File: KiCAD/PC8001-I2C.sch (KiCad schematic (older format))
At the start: 43 parts, among them J1 ADDR-JP, J2 I2C RTC DS3231, J3 I2C OUT, J4 PC8001 Ext Con, J5 I2C ExtOUT1, J6 I2C ExtOUT1, J7 I2C ExtOUT1, J8 I2C ExtOUT1, Q1 2N7000, U1 74HC138, U2 DS1307+, U3 8255, U4 24LC1025, U5 24LC1025, U6 74HC07, U7 74HC4051, U8 74LS32, Y1 32.768kHz

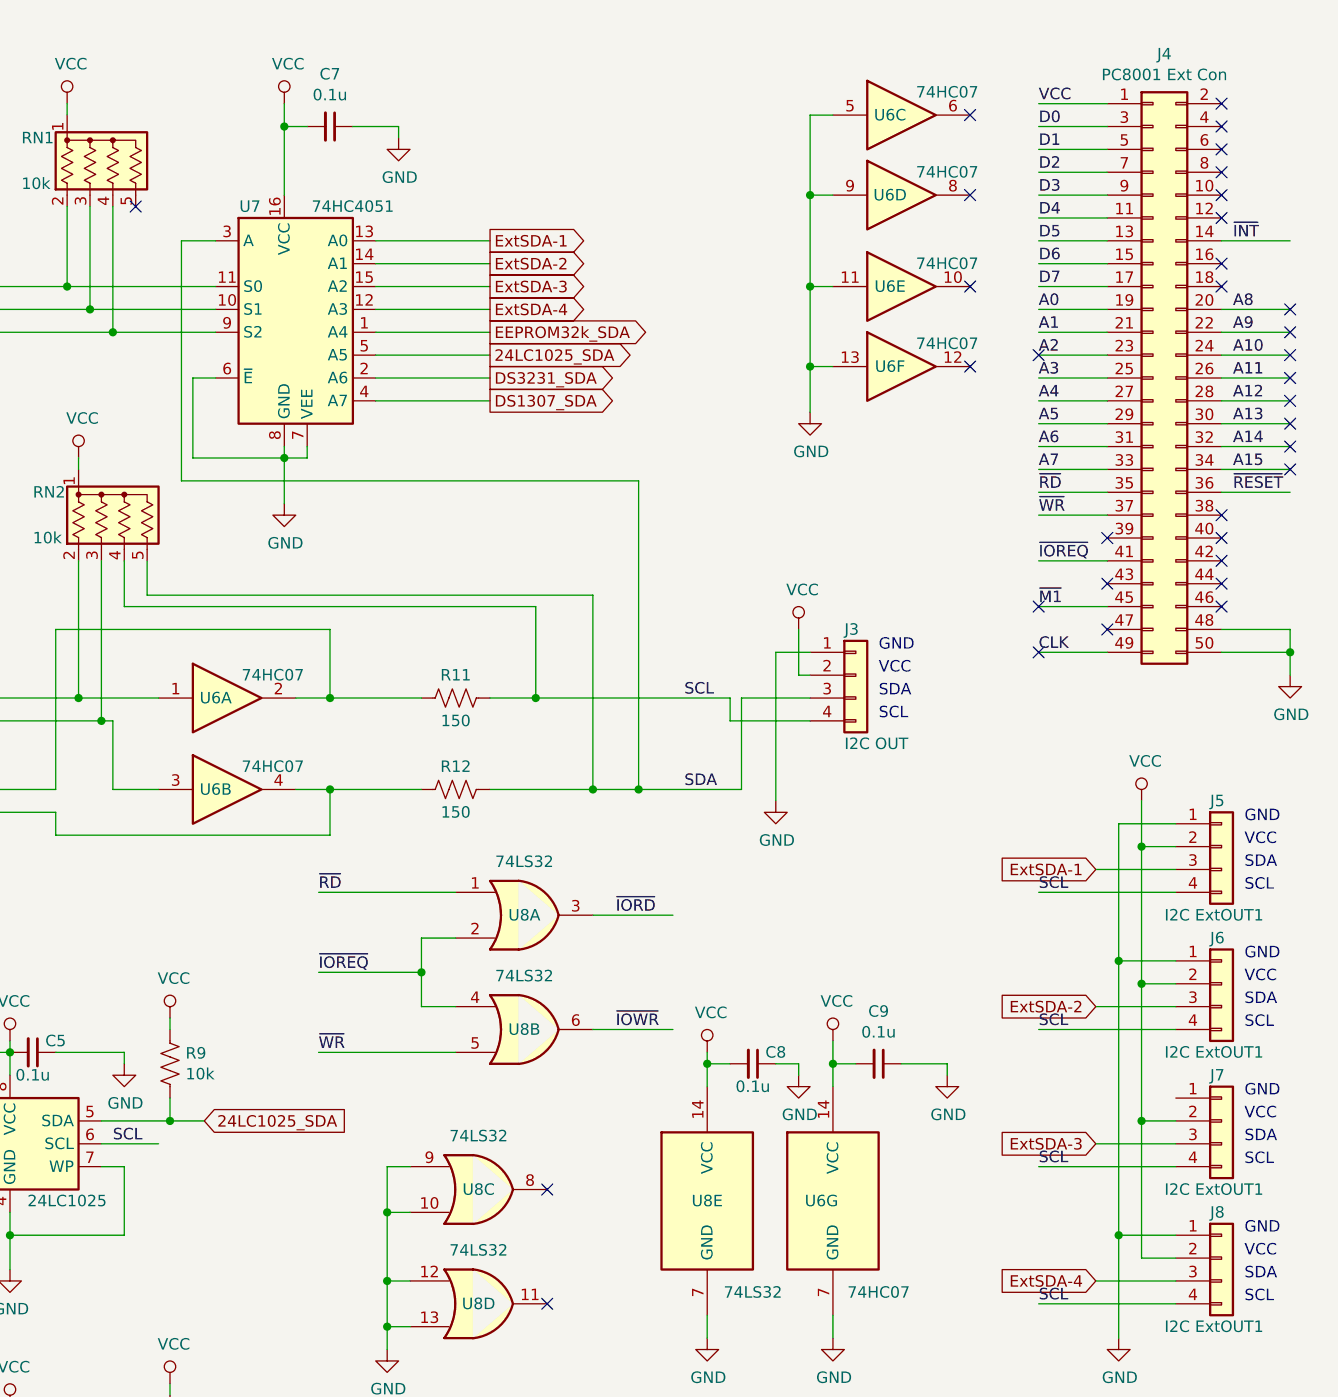
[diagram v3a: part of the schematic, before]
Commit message: 外部I2C端子へ74HC07追加
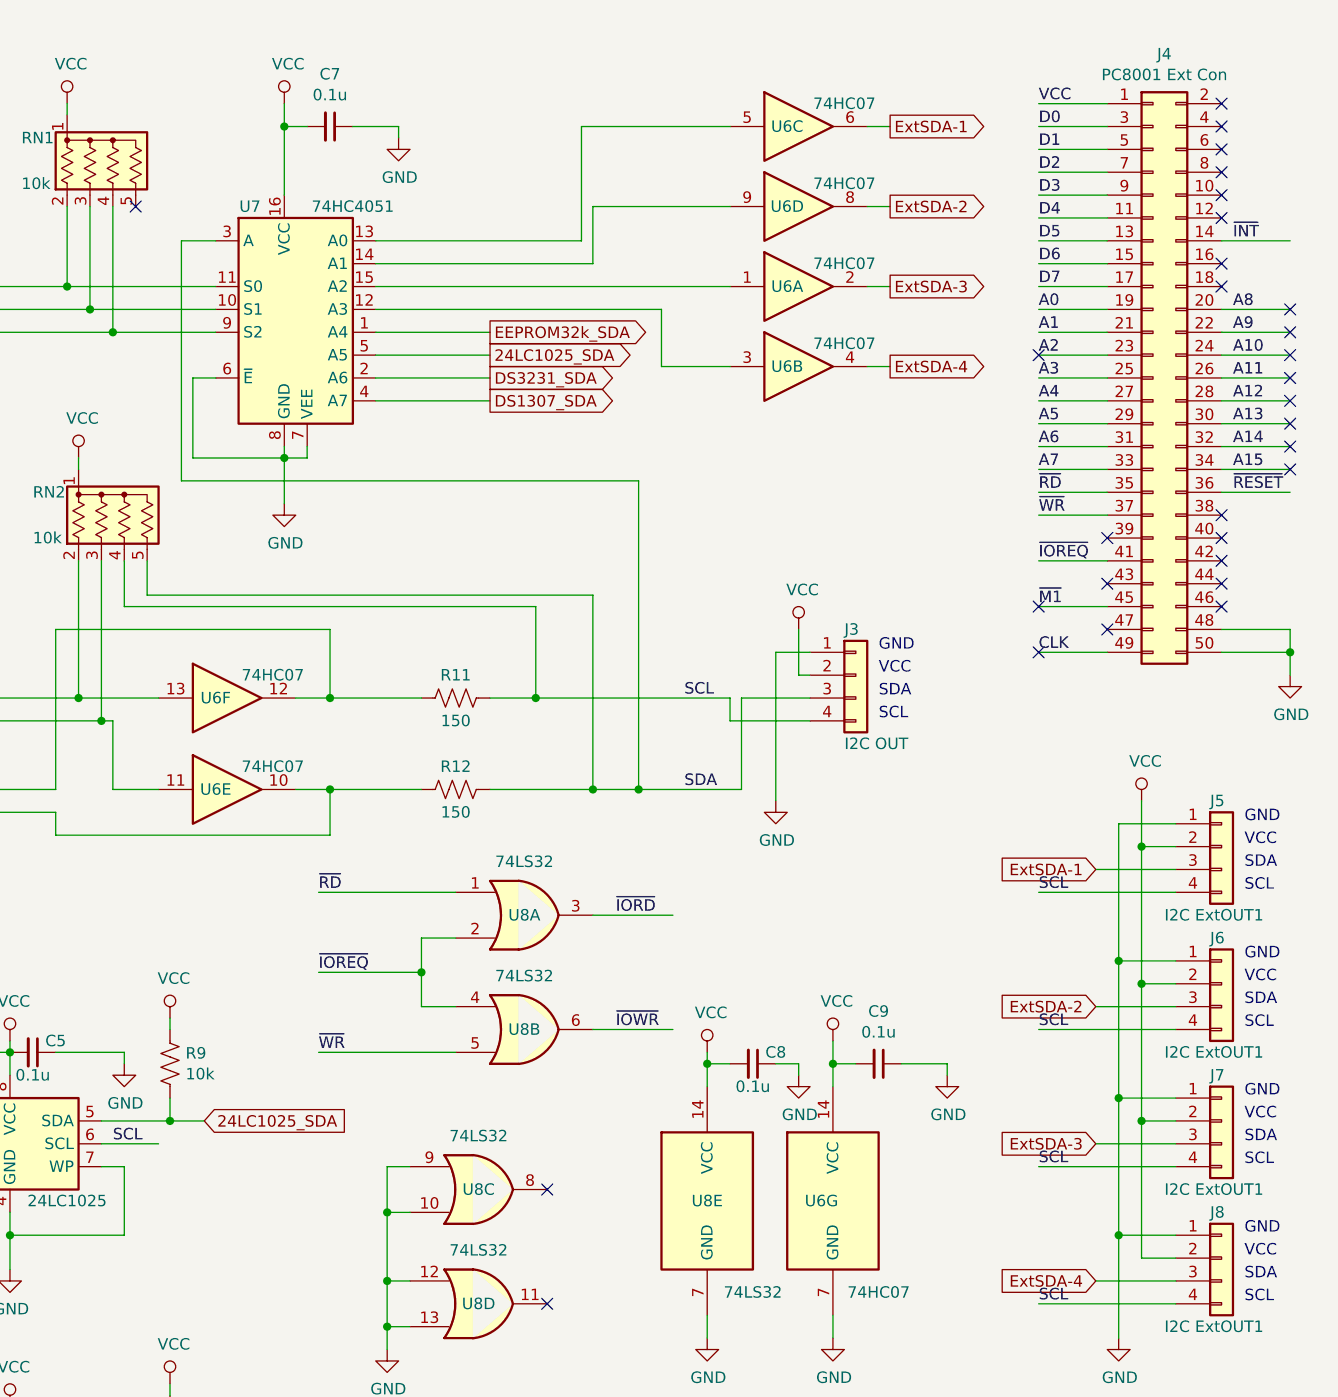
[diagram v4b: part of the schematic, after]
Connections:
- net ExtSDA-1: now also U6.6; no longer U7.13 (A0)
- net ExtSDA-2: now also U6.8; no longer U7.14 (A1)
- net ExtSDA-3: now also U6.2; no longer U7.15 (A2)
- net ExtSDA-4: now also U6.4; no longer U7.12 (A3)
- net GND: now also J7.1 (Pin_1); no longer U6.11, U6.13, U6.5, U6.9
- net at R11.1, U3.13 (PC4): now also U6.12; no longer U6.2
- net at R12.1, U3.12 (PC5): now also U6.10; no longer U6.4
- net at RN2.2 (R1), U3.14 (PC0): now also U6.13; no longer U6.1
- net at RN2.3 (R2), U3.15 (PC1): now also U6.11; no longer U6.3
- new net: U6.1, U7.15 (A2)
- new net: U6.3, U7.12 (A3)
- new net: U6.5, U7.13 (A0)
- new net: U6.9, U7.14 (A1)
- no-connect marks 51 -> 47
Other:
- moved on the sheet: U6A, U6B, U6C, U6D, U6E, U6F
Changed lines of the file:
@@
 Text GLabel 7600 2100 2    50   Output ~ 0
 DS1307_SDA
-Wire Wire Line
-	7100 1700 7600 1700
-Wire Wire Line
-	7100 1600 7600 1600
-Wire Wire Line
-	7100 1500 7600 1500
-Wire Wire Line
-	7100 1400 7600 1400
 Text GLabel 7600 1900 2    50   Output ~ 0
 24LC1025_SDA
@@
 L 74xx:74LS07 U6
 U 1 1 5E8C9365
-P 6450 3400
-F 0 "U6" H 6400 3400 50  0000 C CNN
-F 1 "74HC07" H 6650 3500 50  0000 C CNN
-F 2 "" H 6450 3400 50  0001 C CNN
-F 3 "www.ti.com/lit/ds/symlink/sn74ls07.pdf" H 6450 3400 50  0001 C CNN
-	1    6450 3400
+P 8950 1600
+F 0 "U6" H 8900 1600 50  0000 C CNN
+F 1 "74HC07" H 9150 1700 50  0000 C CNN
+F 2 "" H 8950 1600 50  0001 C CNN
+F 3 "www.ti.com/lit/ds/symlink/sn74ls07.pdf" H 8950 1600 50  0001 C CNN
+	1    8950 1600
 	1    0    0    -1
 $EndComp
@@
 L 74xx:74LS07 U6
 U 2 1 5E8CAB8D
-P 6450 3800
-F 0 "U6" H 6400 3800 50  0000 C CNN
-F 1 "74HC07" H 6650 3900 50  0000 C CNN
-F 2 "" H 6450 3800 50  0001 C CNN
-F 3 "www.ti.com/lit/ds/symlink/sn74ls07.pdf" H 6450 3800 50  0001 C CNN
-	2    6450 3800
+P 8950 1950
+F 0 "U6" H 8900 1950 50  0000 C CNN
+F 1 "74HC07" H 9150 2050 50  0000 C CNN
+F 2 "" H 8950 1950 50  0001 C CNN
+F 3 "www.ti.com/lit/ds/symlink/sn74ls07.pdf" H 8950 1950 50  0001 C CNN
+	2    8950 1950
 	1    0    0    -1
 $EndComp
@@
 L 74xx:74LS07 U6
 U 3 1 5EAEAB10
-P 9400 850
-F 0 "U6" H 9350 850 50  0000 C CNN
-F 1 "74HC07" H 9600 950 50  0000 C CNN
-F 2 "" H 9400 850 50  0001 C CNN
-F 3 "www.ti.com/lit/ds/symlink/sn74ls07.pdf" H 9400 850 50  0001 C CNN
-	3    9400 850
+P 8950 900
+F 0 "U6" H 8900 900 50  0000 C CNN
+F 1 "74HC07" H 9150 1000 50  0000 C CNN
+F 2 "" H 8950 900 50  0001 C CNN
+F 3 "www.ti.com/lit/ds/symlink/sn74ls07.pdf" H 8950 900 50  0001 C CNN
+	3    8950 900
 	1    0    0    -1
 $EndComp
@@
 L 74xx:74LS07 U6
 U 4 1 5EAEB723
-P 9400 1200
-F 0 "U6" H 9350 1200 50  0000 C CNN
-F 1 "74HC07" H 9600 1300 50  0000 C CNN
-F 2 "" H 9400 1200 50  0001 C CNN
-F 3 "www.ti.com/lit/ds/symlink/sn74ls07.pdf" H 9400 1200 50  0001 C CNN
-	4    9400 1200
+P 8950 1250
+F 0 "U6" H 8900 1250 50  0000 C CNN
+F 1 "74HC07" H 9150 1350 50  0000 C CNN
+F 2 "" H 8950 1250 50  0001 C CNN
+F 3 "www.ti.com/lit/ds/symlink/sn74ls07.pdf" H 8950 1250 50  0001 C CNN
+	4    8950 1250
 	1    0    0    -1
 $EndComp
@@
 L 74xx:74LS07 U6
 U 5 1 5EAEBD50
-P 9400 1600
-F 0 "U6" H 9350 1600 50  0000 C CNN
-F 1 "74HC07" H 9600 1700 50  0000 C CNN
-F 2 "" H 9400 1600 50  0001 C CNN
-F 3 "www.ti.com/lit/ds/symlink/sn74ls07.pdf" H 9400 1600 50  0001 C CNN
-	5    9400 1600
+P 6450 3800
+F 0 "U6" H 6400 3800 50  0000 C CNN
+F 1 "74HC07" H 6650 3900 50  0000 C CNN
+F 2 "" H 6450 3800 50  0001 C CNN
+F 3 "www.ti.com/lit/ds/symlink/sn74ls07.pdf" H 6450 3800 50  0001 C CNN
+	5    6450 3800
 	1    0    0    -1
 $EndComp
@@
 L 74xx:74LS07 U6
 U 6 1 5EAEC76D
-P 9400 1950
-F 0 "U6" H 9350 1950 50  0000 C CNN
-F 1 "74HC07" H 9600 2050 50  0000 C CNN
-F 2 "" H 9400 1950 50  0001 C CNN
-F 3 "www.ti.com/lit/ds/symlink/sn74ls07.pdf" H 9400 1950 50  0001 C CNN
-	6    9400 1950
-	1    0    0    -1
-$EndComp
-$Comp
-L power:GND #PWR043
-U 1 1 5EB0599F
-P 9000 2150
-F 0 "#PWR043" H 9000 1900 50  0001 C CNN
-F 1 "GND" H 9005 1977 50  0000 C CNN
-F 2 "" H 9000 2150 50  0001 C CNN
-F 3 "" H 9000 2150 50  0001 C CNN
-	1    9000 2150
-	1    0    0    -1
-$EndComp
-Wire Wire Line
-	9000 850  9100 850
-Wire Wire Line
-	9100 1200 9000 1200
-Connection ~ 9000 1200
-Wire Wire Line
-	9000 1200 9000 850
-Wire Wire Line
-	9000 1950 9100 1950
-Wire Wire Line
-	9000 1200 9000 1600
-Connection ~ 9000 1950
-Wire Wire Line
-	9000 1950 9000 2150
-Wire Wire Line
-	9000 1950 9000 1600
-Wire Wire Line
-	9000 1600 9100 1600
-Connection ~ 9000 1600
-NoConn ~ 9700 850
-NoConn ~ 9700 1200
-NoConn ~ 9700 1600
-NoConn ~ 9700 1950
+P 6450 3400
+F 0 "U6" H 6400 3400 50  0000 C CNN
+F 1 "74HC07" H 6650 3500 50  0000 C CNN
+F 2 "" H 6450 3400 50  0001 C CNN
+F 3 "www.ti.com/lit/ds/symlink/sn74ls07.pdf" H 6450 3400 50  0001 C CNN
+	6    6450 3400
+	1    0    0    -1
+$EndComp
 $Comp
 L 74xx:74LS07 U6
@@
 Wire Wire Line
 	8050 2950 8050 3800
-Text GLabel 7600 1400 2    50   Output ~ 0
+Text GLabel 9350 900  2    50   Output ~ 0
 ExtSDA-1
-Text GLabel 7600 1500 2    50   Output ~ 0
+Text GLabel 9350 1250 2    50   Output ~ 0
 ExtSDA-2
-Text GLabel 7600 1600 2    50   Output ~ 0
+Text GLabel 9350 1600 2    50   Output ~ 0
 ExtSDA-3
-Text GLabel 7600 1700 2    50   Output ~ 0
+Text GLabel 9350 1950 2    50   Output ~ 0
 ExtSDA-4
 Wire Wire Line
@@
 Connection ~ 10350 4550
 Wire Wire Line
-	10350 4550 10350 5750
+	10350 4550 10350 5150
 Wire Wire Line
 	10600 5750 10350 5750
@@
 Wire Wire Line
 	10350 5750 10350 6200
+Wire Wire Line
+	10600 5150 10350 5150
+Connection ~ 10350 5150
+Wire Wire Line
+	10350 5150 10350 5750
+Wire Wire Line
+	9250 900  9350 900
+Wire Wire Line
+	9250 1250 9350 1250
+Wire Wire Line
+	9250 1600 9350 1600
+Wire Wire Line
+	9250 1950 9350 1950
+Wire Wire Line
+	8000 1400 8000 900
+Wire Wire Line
+	8000 900  8650 900
+Wire Wire Line
+	7100 1400 8000 1400
+Wire Wire Line
+	8050 1250 8050 1500
+Wire Wire Line
+	7100 1500 8050 1500
+Wire Wire Line
+	8050 1250 8650 1250
+Wire Wire Line
+	7100 1600 8650 1600
+Wire Wire Line
+	8350 1700 8350 1950
+Wire Wire Line
+	8350 1950 8650 1950
+Wire Wire Line
+	7100 1700 8350 1700
 $EndSCHEMATC

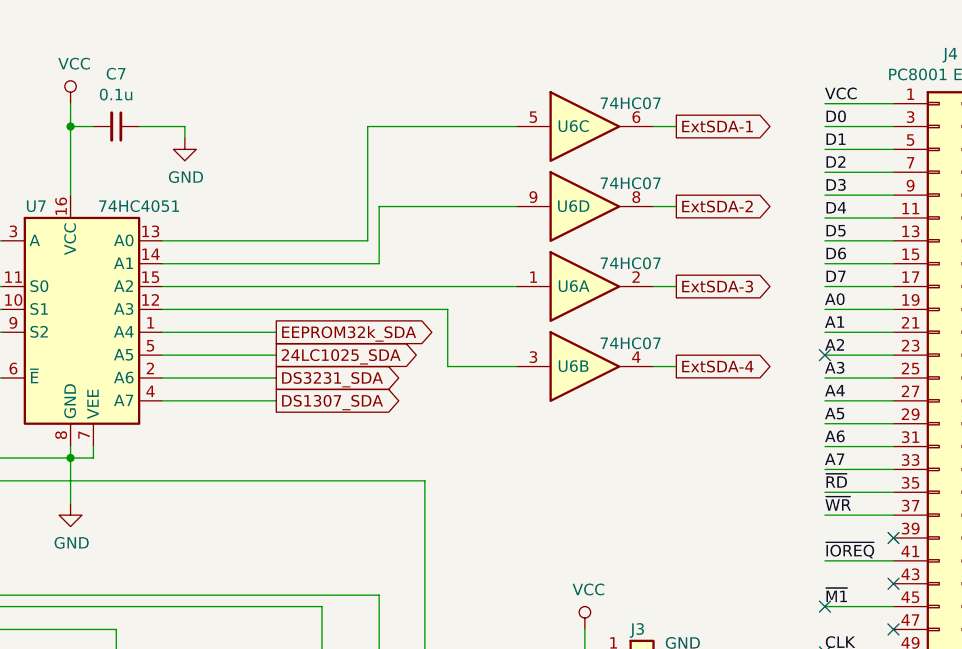
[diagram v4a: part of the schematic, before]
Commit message: REV2基板 ExtSDA関係再検討
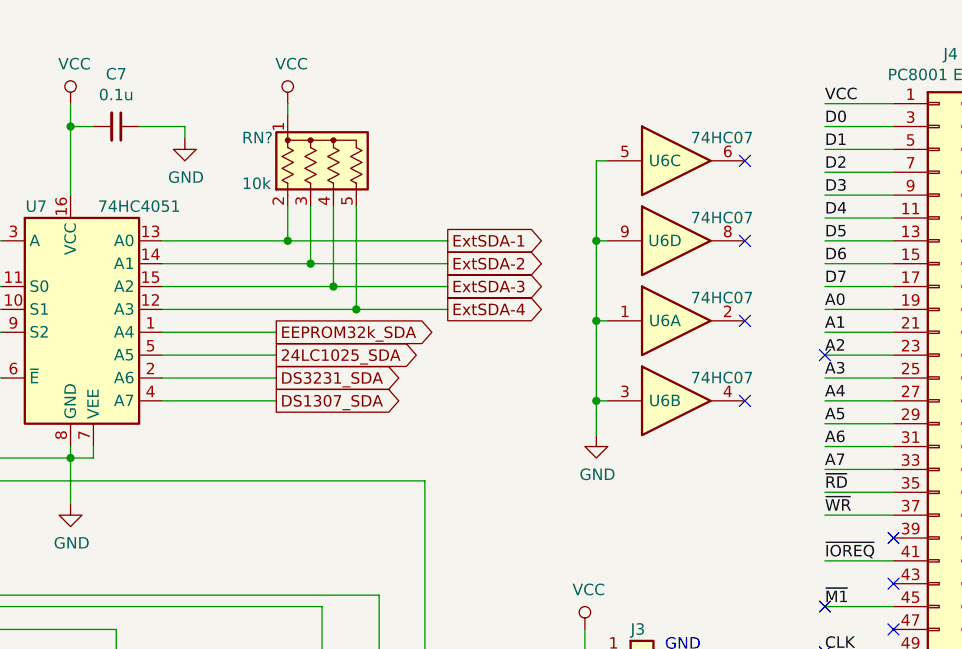
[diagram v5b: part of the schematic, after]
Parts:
- added RN?: 10k, Resistor_THT:R_Array_SIP5, symbol Device:R_Network04_US
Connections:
- net ExtSDA-1: now also U7.13 (A0), RN?.2 (R1); no longer U6.6
- net ExtSDA-2: now also U7.14 (A1), RN?.3 (R2); no longer U6.8
- net ExtSDA-3: now also U7.15 (A2), RN?.4 (R3); no longer U6.2
- net ExtSDA-4: now also U7.12 (A3), RN?.5 (R4); no longer U6.4
- net GND: now also U6.1, U6.3, U6.5, U6.9
- net VCC: now also RN?.1 (common)
- no-connect marks 47 -> 51
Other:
- moved on the sheet: U6A, U6B, U6C, U6D
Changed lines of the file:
@@
 L 74xx:74LS07 U6
 U 1 1 5E8C9365
-P 8950 1600
-F 0 "U6" H 8900 1600 50  0000 C CNN
-F 1 "74HC07" H 9150 1700 50  0000 C CNN
-F 2 "" H 8950 1600 50  0001 C CNN
-F 3 "www.ti.com/lit/ds/symlink/sn74ls07.pdf" H 8950 1600 50  0001 C CNN
-	1    8950 1600
+P 9350 1750
+F 0 "U6" H 9300 1750 50  0000 C CNN
+F 1 "74HC07" H 9550 1850 50  0000 C CNN
+F 2 "" H 9350 1750 50  0001 C CNN
+F 3 "www.ti.com/lit/ds/symlink/sn74ls07.pdf" H 9350 1750 50  0001 C CNN
+	1    9350 1750
 	1    0    0    -1
 $EndComp
@@
 L 74xx:74LS07 U6
 U 2 1 5E8CAB8D
-P 8950 1950
-F 0 "U6" H 8900 1950 50  0000 C CNN
-F 1 "74HC07" H 9150 2050 50  0000 C CNN
-F 2 "" H 8950 1950 50  0001 C CNN
-F 3 "www.ti.com/lit/ds/symlink/sn74ls07.pdf" H 8950 1950 50  0001 C CNN
-	2    8950 1950
+P 9350 2100
+F 0 "U6" H 9300 2100 50  0000 C CNN
+F 1 "74HC07" H 9550 2200 50  0000 C CNN
+F 2 "" H 9350 2100 50  0001 C CNN
+F 3 "www.ti.com/lit/ds/symlink/sn74ls07.pdf" H 9350 2100 50  0001 C CNN
+	2    9350 2100
 	1    0    0    -1
 $EndComp
@@
 L 74xx:74LS07 U6
 U 3 1 5EAEAB10
-P 8950 900
-F 0 "U6" H 8900 900 50  0000 C CNN
-F 1 "74HC07" H 9150 1000 50  0000 C CNN
-F 2 "" H 8950 900 50  0001 C CNN
-F 3 "www.ti.com/lit/ds/symlink/sn74ls07.pdf" H 8950 900 50  0001 C CNN
-	3    8950 900
+P 9350 1050
+F 0 "U6" H 9300 1050 50  0000 C CNN
+F 1 "74HC07" H 9550 1150 50  0000 C CNN
+F 2 "" H 9350 1050 50  0001 C CNN
+F 3 "www.ti.com/lit/ds/symlink/sn74ls07.pdf" H 9350 1050 50  0001 C CNN
+	3    9350 1050
 	1    0    0    -1
 $EndComp
@@
 L 74xx:74LS07 U6
 U 4 1 5EAEB723
-P 8950 1250
-F 0 "U6" H 8900 1250 50  0000 C CNN
-F 1 "74HC07" H 9150 1350 50  0000 C CNN
-F 2 "" H 8950 1250 50  0001 C CNN
-F 3 "www.ti.com/lit/ds/symlink/sn74ls07.pdf" H 8950 1250 50  0001 C CNN
-	4    8950 1250
+P 9350 1400
+F 0 "U6" H 9300 1400 50  0000 C CNN
+F 1 "74HC07" H 9550 1500 50  0000 C CNN
+F 2 "" H 9350 1400 50  0001 C CNN
+F 3 "www.ti.com/lit/ds/symlink/sn74ls07.pdf" H 9350 1400 50  0001 C CNN
+	4    9350 1400
 	1    0    0    -1
 $EndComp
@@
 Wire Wire Line
 	8050 2950 8050 3800
-Text GLabel 9350 900  2    50   Output ~ 0
+Text GLabel 8350 1400 2    50   Output ~ 0
 ExtSDA-1
-Text GLabel 9350 1250 2    50   Output ~ 0
+Text GLabel 8350 1500 2    50   Output ~ 0
 ExtSDA-2
-Text GLabel 9350 1600 2    50   Output ~ 0
+Text GLabel 8350 1600 2    50   Output ~ 0
 ExtSDA-3
-Text GLabel 9350 1950 2    50   Output ~ 0
+Text GLabel 8350 1700 2    50   Output ~ 0
 ExtSDA-4
 Wire Wire Line
@@
 	10350 5150 10350 5750
 Wire Wire Line
-	9250 900  9350 900
-Wire Wire Line
-	9250 1250 9350 1250
-Wire Wire Line
-	9250 1600 9350 1600
-Wire Wire Line
-	9250 1950 9350 1950
-Wire Wire Line
-	8000 1400 8000 900
-Wire Wire Line
-	8000 900  8650 900
-Wire Wire Line
-	7100 1400 8000 1400
-Wire Wire Line
-	8050 1250 8050 1500
-Wire Wire Line
-	7100 1500 8050 1500
-Wire Wire Line
-	8050 1250 8650 1250
-Wire Wire Line
-	7100 1600 8650 1600
-Wire Wire Line
-	8350 1700 8350 1950
-Wire Wire Line
-	8350 1950 8650 1950
-Wire Wire Line
-	7100 1700 8350 1700
+	7100 1400 7650 1400
+Wire Wire Line
+	7100 1500 7750 1500
+Wire Wire Line
+	7100 1700 7950 1700
+Wire Wire Line
+	7100 1600 7850 1600
+$Comp
+L Device:R_Network04_US RN?
+U 1 1 5F78F1BE
+P 7850 1050
+F 0 "RN?" H 7450 1150 50  0000 L CNN
+F 1 "10k" H 7450 950 50  0000 L CNN
+F 2 "Resistor_THT:R_Array_SIP5" V 8125 1050 50  0001 C CNN
+F 3 "http://www.vishay.com/docs/31509/csc.pdf" H 7850 1050 50  0001 C CNN
+	1    7850 1050
+	1    0    0    -1
+$EndComp
+$Comp
+L power:VCC #PWR?
+U 1 1 5F78FA25
+P 7650 800
+F 0 "#PWR?" H 7650 650 50  0001 C CNN
+F 1 "VCC" H 7667 973 50  0000 C CNN
+F 2 "" H 7650 800 50  0001 C CNN
+F 3 "" H 7650 800 50  0001 C CNN
+	1    7650 800
+	1    0    0    -1
+$EndComp
+Wire Wire Line
+	7650 800  7650 850
+Wire Wire Line
+	7650 1250 7650 1400
+Connection ~ 7650 1400
+Wire Wire Line
+	7650 1400 8350 1400
+Wire Wire Line
+	7750 1250 7750 1500
+Connection ~ 7750 1500
+Wire Wire Line
+	7750 1500 8350 1500
+Wire Wire Line
+	7850 1250 7850 1600
+Connection ~ 7850 1600
+Wire Wire Line
+	7850 1600 8350 1600
+Wire Wire Line
+	7950 1250 7950 1700
+Connection ~ 7950 1700
+Wire Wire Line
+	7950 1700 8350 1700
+$Comp
+L power:GND #PWR?
+U 1 1 5F8250D8
+P 9000 2250
+F 0 "#PWR?" H 9000 2000 50  0001 C CNN
+F 1 "GND" H 9005 2077 50  0000 C CNN
+F 2 "" H 9000 2250 50  0001 C CNN
+F 3 "" H 9000 2250 50  0001 C CNN
+	1    9000 2250
+	1    0    0    -1
+$EndComp
+Wire Wire Line
+	9050 1050 9000 1050
+Wire Wire Line
+	9000 1050 9000 1400
+Wire Wire Line
+	9000 2100 9050 2100
+Connection ~ 9000 2100
+Wire Wire Line
+	9000 2100 9000 2250
+Wire Wire Line
+	9050 1750 9000 1750
+Connection ~ 9000 1750
+Wire Wire Line
+	9000 1750 9000 2100
+Wire Wire Line
+	9050 1400 9000 1400
+Connection ~ 9000 1400
+Wire Wire Line
+	9000 1400 9000 1750
+NoConn ~ 9650 1050
+NoConn ~ 9650 1400
+NoConn ~ 9650 1750
+NoConn ~ 9650 2100
 $EndSCHEMATC
